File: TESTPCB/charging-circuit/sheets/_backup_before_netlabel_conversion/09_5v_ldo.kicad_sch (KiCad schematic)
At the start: 9 parts, among them P7 1.27mm/1*3p, U6 MT3608

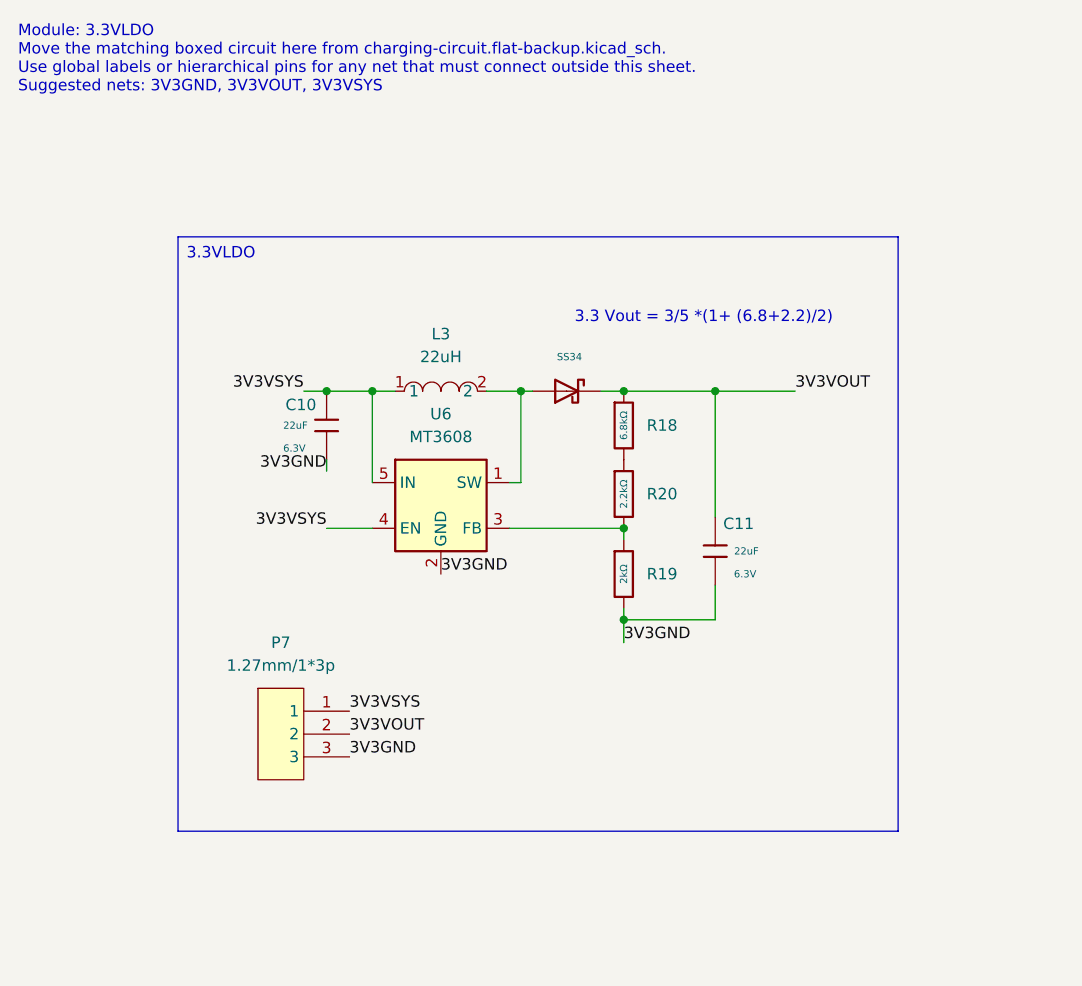
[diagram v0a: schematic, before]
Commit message: Fixed formatting issues, now the hierachal sheets are all labeled as net labels and when we want to expose their pins we will make them into hierchal or global pins
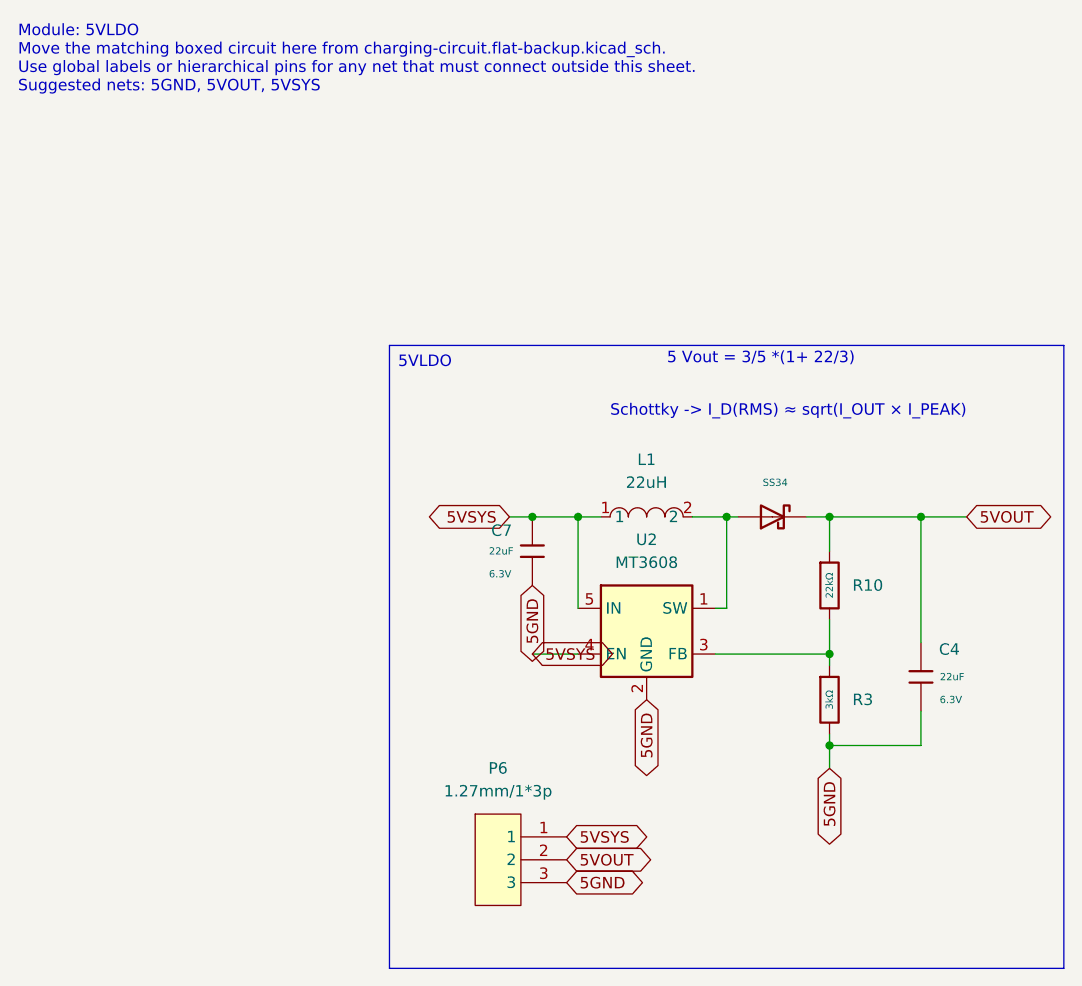
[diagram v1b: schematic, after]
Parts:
- removed C10, C11: 22uF, PCM_JLCPCB:C_0603, symbol PCM_JLCPCB-Capacitors:0603,22uF
- removed D6: SS34, PCM_JLCPCB:D_SMA, symbol PCM_JLCPCB-Diodes:Schottky,SS34
- removed L3: 22uH, easyeda2kicad:IND-SMD_L7.5-W7.5, symbol easyeda2kicad:CYH74-22UH
- removed P7: 1.27mm/1*3p, easyeda2kicad:HDR-TH_3P-P1.27-V-M-1, symbol easyeda2kicad:1.27mm_1*3p
- removed R18: 6.8kΩ, PCM_JLCPCB:R_0603, symbol PCM_JLCPCB-Resistors:0603,22kΩ
- removed R19: 2kΩ, PCM_JLCPCB:R_0603, symbol PCM_JLCPCB-Resistors:0603,3kΩ
- removed R20: 2.2kΩ, PCM_JLCPCB:R_0603, symbol PCM_JLCPCB-Resistors:0603,22kΩ
- removed U6: MT3608, PCM_JLCPCB:SOT-23-6_L2.9-W1.6-P0.95-LS2.8-BL, symbol Regulator_Switching:MT3608
- added C4, C7: 22uF, PCM_JLCPCB:C_0603, symbol PCM_JLCPCB-Capacitors:0603,22uF
- added D5: SS34, PCM_JLCPCB:D_SMA, symbol PCM_JLCPCB-Diodes:Schottky,SS34
- added L1: 22uH, easyeda2kicad:IND-SMD_L7.5-W7.5, symbol easyeda2kicad:CYH74-22UH
- added P6: 1.27mm/1*3p, easyeda2kicad:HDR-TH_3P-P1.27-V-M-1, symbol easyeda2kicad:1.27mm_1*3p
- added R10: 22kΩ, PCM_JLCPCB:R_0603, symbol PCM_JLCPCB-Resistors:0603,22kΩ
- added R3: 3kΩ, PCM_JLCPCB:R_0603, symbol PCM_JLCPCB-Resistors:0603,3kΩ
- added U2: MT3608, easyeda2kicad:SOT-23-6_L2.9-W1.6-P0.95-LS2.8-BL, symbol Regulator_Switching:MT3608
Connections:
- new net: D5.2, L1.2, U2.1 (SW)
- new net: R10.2, R3.1, U2.3 (FB)
- new net 5GND: C4.1, C7.2, P6.3, R3.2, U2.2 (GND)
- new net 5VOUT: C4.2, D5.1, P6.2, R10.1
- new net 5VSYS: C7.1, L1.1, P6.1, U2.4 (EN), U2.5 (IN)
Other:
- note added: "5 Vout = 3/5 *(1+ 22/3)"
- note added: "Module: 5VLDO Move the matching boxed circuit here from charging-circuit.flat-backup.kicad_sch. Use global labels or hierarchical pins for any net that must connect outside this sheet. Suggested nets: 5GND, 5VOUT, 5VSYS"
- note added: "Schottky -> I_D(RMS) ≈ sqrt(I_OUT × I_PEAK)"
- note removed: "3.3 Vout = 3/5 *(1+ (6.8+2.2)/2)"
- note removed: "Module: 3.3VLDO Move the matching boxed circuit here from charging-circuit.flat-backup.kicad_sch. Use global labels or hierarchical pins for any net that must connect outside this sheet. Suggested nets: 3V3GND, 3V3VOUT, 3V3VSYS"
